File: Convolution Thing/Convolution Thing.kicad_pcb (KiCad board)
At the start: 2 copper layers, 205 parts, among them IC1 PCM3060PW, IC2 SN74LVC1G07DCK3, IC3 LP55231, J1 Eurorack power, J10 In CV 3, J11 In CV 4, J12 In CV 5, J13 In CV 6, J14 In CV 7, J15 In CV 8, J16 LED Header, J17 USB_A, J18 Gate In 1, J19 Gate In 2, J2 Power Header, J20 Gate In 3, J21 Gate In 4, J22 CM4 Pins 1-100, J23 CM4 Pins 101-200, J24 OLED Pins 1-20, J25 OLED Pins 21-40, J3 GPIO Header, J4 Out Left, J5 Out Right, J6 In Left, J7 In Right, J8 In CV 1, J9 In CV 2, Q1 NPN, Q2 NPN, Q3 NPN, Q4 NPN, U1 Compute Module 4, U10 LM4040DBZ-2.5, U11 LM4040DBZ-2.5, U2 TLV1117-50, U3 ADP2303ARDZ-5.0, U4 NE5532, U5 NE5532, U6 NE5532, U7 LTC2309_TSSOP, U8 MCP6004, U9 MCP6004

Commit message: PCB layout work and related changes to the schematic
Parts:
- removed the C13 at (89.5, 92.8)
- removed the C16 at (98.7, 82.3)
- removed the C17 at (180.0, 137.4)
- removed the C18 at (218.5, 117.6)
- removed the C27 at (267.1, 26.6)
- removed the C33 at (187.7, 82.3)
- removed the C34 at (187.7, 85.4)
- removed the C35 at (192.2, 82.3)
- removed the C36 at (187.7, 88.4)
- removed the C52 at (167.6, 69.9)
- removed the C53 at (207.9, 29.6)
- removed the C61 at (167.6, 66.9)
- removed the C64 at (88.9, 144.6)
- removed the C8 at (88.9, 96.4)
- removed the J15 at (144.2, 34.2)
- removed the J20 at (230.4, 156.5)
- removed the J21 at (249.3, 136.8)
- removed the R2 at (188.9, 136.7)
- removed the R21 at (267.1, 32.6)
- removed the R22 at (192.2, 85.3)
- removed the R3 at (189.1, 133.6)
- removed the TP10 at (248.7, 78.5)
- removed the TP8 at (258.8, 78.5)
- removed the U2 at (70.4, 112.4)
- removed the U6 at (231.3, 42.9)
- added C19: 100nF, Capacitor_SMD:C_0805_2012Metric, F.Cu at (227.9, 221.3)
- added C25: 10uF, Capacitor_SMD:C_0805_2012Metric, F.Cu at (157.6, 235.1)
- added C26: 330pF, Capacitor_SMD:C_0805_2012Metric, F.Cu at (158.1, 216.1)
- added C31: 100nF, Capacitor_SMD:C_0805_2012Metric, F.Cu at (22.6, 35.5)
- added C32: 2.2uF, Capacitor_SMD:C_0805_2012Metric, F.Cu at (18.1, 41.6)
- added C57: 100nF, Capacitor_SMD:C_0805_2012Metric, F.Cu at (237.4, 119.1)
- added C59: 470nF, Capacitor_SMD:C_0805_2012Metric, F.Cu at (43.4, 132.5)
- added C60: 100nF, Capacitor_SMD:C_0805_2012Metric, F.Cu at (41.2, 135.6)
- added C65: 100nF, Capacitor_SMD:C_0805_2012Metric, F.Cu at (27.4, 155.3)
- added C66: 100nF, Capacitor_SMD:C_0805_2012Metric, F.Cu at (30.9, 164.5)
- added C67: 10uF, Capacitor_SMD:C_0805_2012Metric, F.Cu at (30.9, 162.5)
- added C9: 100nF, Capacitor_SMD:C_0805_2012Metric, F.Cu at (163.1, 167.4)
- added D10: LED 7, LED_SMD:LED_0805_2012Metric, F.Cu at (53.6, 125.2)
- added D11: LED 8, LED_SMD:LED_0805_2012Metric, F.Cu at (55.7, 125.2)
- added D12: LED 9, LED_SMD:LED_0805_2012Metric, F.Cu at (57.8, 125.2)
- added D13: Activity LED, LED_SMD:LED_0805_2012Metric, F.Cu at (33.4, 116.5)
- added D14: Power LED, LED_SMD:LED_0805_2012Metric, F.Cu at (38.0, 112.8)
- added D6: LED 3, LED_SMD:LED_0805_2012Metric, F.Cu at (45.2, 125.2)
- added D7: LED 4, LED_SMD:LED_0805_2012Metric, F.Cu at (47.3, 125.2)
- added D8: LED 5, LED_SMD:LED_0805_2012Metric, F.Cu at (49.4, 125.2)
- added D9: LED 6, LED_SMD:LED_0805_2012Metric, F.Cu at (51.5, 125.2)
- added J17: Gate In 2, Connector_Audio:Jack_3.5mm_QingPu_WQP-PJ398SM_Vertical_CircularHoles, F.Cu at (80.9, -14.8)
- added J24: GPIO Header, Connector_PinHeader_2.54mm:PinHeader_2x07_P2.54mm_Vertical, F.Cu at (72.1, 160.8)
- added R18: 100k, Resistor_SMD:R_0805_2012Metric, F.Cu at (157.6, 228.5)
- added R19: 22k, Resistor_SMD:R_0805_2012Metric, F.Cu at (158.1, 223.2)
- added R55: 100, Resistor_SMD:R_0805_2012Metric, F.Cu at (42.4, 112.8)
- added R56: 100, Resistor_SMD:R_0805_2012Metric, F.Cu at (33.3, 119.5)
- added TP16: CV4 TP, TestPoint:TestPoint_Loop_D2.60mm_Drill1.6mm_Beaded, F.Cu at (300.2, 91.8)
- added TP18: CV6 TP, TestPoint:TestPoint_Loop_D2.60mm_Drill1.6mm_Beaded, F.Cu at (303.3, 142.7)
- added TP19: CV_SCL TP, TestPoint:TestPoint_Loop_D2.60mm_Drill1.6mm_Beaded, F.Cu at (70.0, 33.7)
- added TP2: PCM_FS TP, TestPoint:TestPoint_Loop_D2.60mm_Drill1.6mm_Beaded, F.Cu at (75.1, 20.5)
- added TP20: CV_SDA TP, TestPoint:TestPoint_Loop_D2.60mm_Drill1.6mm_Beaded, F.Cu at (65.0, 33.7)
- added TP21: CV7 TP, TestPoint:TestPoint_Loop_D2.60mm_Drill1.6mm_Beaded, F.Cu at (263.2, 186.8)
- added TP22: CV8 TP, TestPoint:TestPoint_Loop_D2.60mm_Drill1.6mm_Beaded, F.Cu at (304.1, 187.8)
- added TP25: LED_SCL TP, TestPoint:TestPoint_Loop_D2.60mm_Drill1.6mm_Beaded, F.Cu at (81.9, 28.4)
- added TP26: LED_SDA TP, TestPoint:TestPoint_Loop_D2.60mm_Drill1.6mm_Beaded, F.Cu at (81.9, 33.4)
- added TP28: Gate 2 TP, TestPoint:TestPoint_Loop_D2.60mm_Drill1.6mm_Beaded, F.Cu at (81.9, -20.7)
- added TP29: Gate 3 TP, TestPoint:TestPoint_Loop_D2.60mm_Drill1.6mm_Beaded, F.Cu at (101.2, -20.4)
- added TP30: Gate 4 TP, TestPoint:TestPoint_Loop_D2.60mm_Drill1.6mm_Beaded, F.Cu at (119.2, -19.9)
- added TP31: +3.3V TP, TestPoint:TestPoint_Loop_D2.60mm_Drill1.6mm_Beaded, F.Cu at (63.0, 154.5)
- added U10: Compute Module 4, CM4:Raspberry-Pi-4-Compute-Module, F.Cu at (38.6, 176.4)
- C10: value 100nF -> 22uF
- C12: value 22uF -> 100uF; footprint Capacitor_SMD:C_0805_2012Metric -> Capacitor_SMD:C_1210_3225Metric
- C14: value 10uF -> 47uF
- C23, C7: value 100nF -> 10uF
- C29: value 10uF -> 100nF
- C30: value 330pF -> 2.2uF
- C63: value 470nF -> 100nF
- D4: value Activity LED -> LED 1
- D5: value Power LED -> LED 2
- IC2: value SN74LVC1G07DCK3 -> LP55231; footprint SamacSys:SOT65P210X110-5N -> SamacSys:QFN50P400X400X80-25N
- IC3: value LP55231 -> SN74LVC1G07DCK3; footprint SamacSys:QFN50P400X400X80-25N -> SamacSys:SOT65P210X110-5N
- J1: footprint Connector_PinHeader_2.54mm:PinHeader_2x10_P2.54mm_Vertical_SMD -> Connector_PinHeader_2.54mm:PinHeader_2x05_P2.54mm_Vertical_SMD
- J10: value In CV 3 -> In CV 4; footprint SamacSys:ACJMNV352S -> Connector_Audio:Jack_3.5mm_QingPu_WQP-PJ398SM_Vertical_CircularHoles
- J11: value In CV 4 -> In CV 5; footprint SamacSys:ACJMNV352S -> Connector_Audio:Jack_3.5mm_QingPu_WQP-PJ398SM_Vertical_CircularHoles
- J12: value In CV 5 -> In CV 6; footprint SamacSys:ACJMNV352S -> Connector_Audio:Jack_3.5mm_QingPu_WQP-PJ398SM_Vertical_CircularHoles
- J13: value In CV 6 -> In CV 7; footprint SamacSys:ACJMNV352S -> Connector_Audio:Jack_3.5mm_QingPu_WQP-PJ398SM_Vertical_CircularHoles
- J14: value In CV 7 -> In CV 8; footprint SamacSys:ACJMNV352S -> Connector_Audio:Jack_3.5mm_QingPu_WQP-PJ398SM_Vertical_CircularHoles
- J16: value LED Header -> Gate In 1; footprint Connector_PinHeader_2.54mm:PinHeader_1x09_P2.54mm_Vertical -> Connector_Audio:Jack_3.5mm_QingPu_WQP-PJ398SM_Vertical_CircularHoles
- J18: value Gate In 1 -> Gate In 3; footprint SamacSys:ACJMNV352S -> Connector_Audio:Jack_3.5mm_QingPu_WQP-PJ398SM_Vertical_CircularHoles
- J19: value Gate In 2 -> Gate In 4; footprint SamacSys:ACJMNV352S -> Connector_Audio:Jack_3.5mm_QingPu_WQP-PJ398SM_Vertical_CircularHoles
- J3: value GPIO Header -> Out Left; footprint Connector_PinSocket_2.54mm:PinSocket_1x15_P2.54mm_Vertical -> Connector_Audio:Jack_3.5mm_QingPu_WQP-PJ398SM_Vertical_CircularHoles
- J4: value Out Left -> Out Right; footprint SamacSys:ACJMNV352S -> Connector_Audio:Jack_3.5mm_QingPu_WQP-PJ398SM_Vertical_CircularHoles
- J5: value Out Right -> In Left; footprint SamacSys:ACJMNV352S -> Connector_Audio:Jack_3.5mm_QingPu_WQP-PJ398SM_Vertical_CircularHoles
- J6: value In Left -> In Right; footprint SamacSys:ACJMNV352S -> Connector_Audio:Jack_3.5mm_QingPu_WQP-PJ398SM_Vertical_CircularHoles
- J7: value In Right -> In CV 1; footprint SamacSys:ACJMNV352S -> Connector_Audio:Jack_3.5mm_QingPu_WQP-PJ398SM_Vertical_CircularHoles
- J8: value In CV 1 -> In CV 2; footprint SamacSys:ACJMNV352S -> Connector_Audio:Jack_3.5mm_QingPu_WQP-PJ398SM_Vertical_CircularHoles
- J9: value In CV 2 -> In CV 3; footprint SamacSys:ACJMNV352S -> Connector_Audio:Jack_3.5mm_QingPu_WQP-PJ398SM_Vertical_CircularHoles
- R20: value 100k -> 910k
- TP1: value +5VA TP -> PCM_CLK TP
- TP10: renamed from TP16; value IN L TP -> IN R TP
- TP11: value CV_SCL TP -> DISPLAY_SCL TP
- TP12: value CV_SDA TP -> DISPLAY_SDA TP
- TP13: value CV_SCL TP -> CV1 TP
- TP14: value CV_SDA TP -> CV2 TP
- TP15: value IN L TP -> CV3 TP
- TP17: value CV1 TP -> CV5 TP
- TP27: renamed from TP20; value Gate TP -> Gate 1 TP
- TP3: value PCM_CLK TP -> PCM_DIN TP
- TP4: value PCM_FS TP -> PCM_DOUT TP
- TP5: value PCM_DIN TP -> CODEC_SDA TP
- TP6: value PCM_DOUT TP -> CODEC_SCL TP
- TP7: value CODEC_SDA TP -> +5VA TP
- TP9: value DISPLAY_SCL TP -> IN L TP
- U1: value Compute Module 4 -> TLV1117-50; footprint CM4:Raspberry-Pi-4-Compute-Module -> Package_TO_SOT_SMD:SOT-223
- moved C30 253.7 mm to (18.1, 38.6)
- moved R20 249.1 mm to (22.5, 38.5)
- moved C29 249.1 mm to (18.1, 35.5)
- moved R57 245.8 mm to (70.0, -4.15)
- moved TP27 241.9 mm to (61.3, -20.7)
- moved R61 239.6 mm to (70.2, -15.1)
- moved Q1 231.0 mm to (70.0, -9.48)
- moved R62 227.1 mm to (90.3, -16.3)
- moved J18 226.0 mm to (100.7, -14.8)
- moved R16 223.0 mm to (138.3, 228.0)
- moved R63 220.0 mm to (109.6, -16.1)
- moved Q2 217.5 mm to (89.5, -9.99)
- moved R58 216.5 mm to (89.3, -4.40)
- moved R14 215.2 mm to (248.7, 230.3)
- moved Q3 213.9 mm to (109.3, -9.99)
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- renumbered C15 to C13, C19 to C15, C20 to C16, C21 to C17, C22 to C18, C24 to C20, C25 to C21, C26 to C22, C28 to C24, C31 to C27, C32 to C28, C37 to C33, C38 to C34, C39 to C35, C40 to C36, C41 to C37, C42 to C38, C43 to C39, C44 to C40, C45 to C41, C46 to C42, C47 to C43, C48 to C44, C49 to C45, C50 to C46, C51 to C47, C54 to C50, C55 to C51, C56 to C52, C57 to C53, C59 to C54, C60 to C55, C58 to C56, C62 to C58, C65 to C61, C66 to C62, C67 to C64, C9 to C8, J17 to J15, J22 to J20, J23 to J21, J24 to J22, J25 to J23, R12 to R10, R13 to R11, R14 to R12, R15 to R13, R16 to R14, R17 to R15, R18 to R16, R19 to R17, R4 to R2, R23 to R21, R24 to R22, R25 to R23, R26 to R24, R27 to R25, R28 to R26, R29 to R27, R30 to R28, R31 to R29, R5 to R3, R32 to R30, R33 to R31, R34 to R32, R35 to R33, R36 to R34, R37 to R35, R38 to R36, R39 to R37, R40 to R38, R41 to R39, R6 to R4, R42 to R40, R43 to R41, R44 to R42, R45 to R43, R46 to R44, R47 to R45, R48 to R46, R49 to R47, R50 to R48, R51 to R49, R7 to R5, R52 to R50, R53 to R51, R54 to R52, R55 to R53, R56 to R54, R8 to R6, R9 to R7, R10 to R8, R11 to R9, TP18 to TP23, TP19 to TP24, TP2 to TP8, U3 to U2, U4 to U3, U5 to U4, U7 to U5, U8 to U6, U9 to U7, U10 to U8, U11 to U9
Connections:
- net DAC_VOUT_L+ renamed CODEC_VOUT_L+
- net DAC_VOUT_L- renamed CODEC_VOUT_L-
- net DAC_VOUT_R+ renamed CODEC_VOUT_R+
- net DAC_VOUT_R- renamed CODEC_VOUT_R-
- C11 pad 1: +12V -> GND
- C11 pad 2: GND -> -12V
- C12 pad 1: GND -> +5VA
- C12 pad 2: -12V -> GND
- C14 pad 1: +3V3 -> +5V
- C23 pad 1: -12V -> Net-(C23-Pad1)
- C23 pad 2: GND -> /Audio In/IN_L
- C24 pad 1: ADC_VIN_L -> CODEC_VIN_L
- C29 pad 1: Net-(C29-Pad1) -> +12V
- C29 pad 2: Net-(C29-Pad2) -> GND
- C30 pad 1: ADC_VIN_R -> +12V
- C30 pad 2: Net-(C30-Pad2) -> GND
- C33 pad 1: Net-(C37-Pad1) -> Net-(C33-Pad1)
- C63 pad 1: /LEDs/C2- -> +3V3
- C63 pad 2: /LEDs/C2+ -> GND
- C7 pad 1: +5V -> +12V
- D4 pad 1: Net-(D4-Pad1) -> GND
- D4 pad 2: +3V3 -> /LEDs/D1
- D5 pad 1: Net-(D5-Pad1) -> GND
- D5 pad 2: +3V3 -> /LEDs/D2
- DS1 pad 32: DISPLAY_SCL -> CM4_SCL1
- DS1 pad 33: DISPLAY_SDA -> CM4_SDA1
- DS1 pad 34: DISPLAY_SDA -> CM4_SDA1
- IC1 pad 1: CODEC_SCL -> CM4_SCL0
- IC1 pad 12: DAC_IN -> CM4_PCM_DOUT
- IC1 pad 2: CODEC_SDA -> CM4_SDA0
- IC1 pad 25: ADC_VIN_L -> CODEC_VIN_L
- IC1 pad 26: ADC_VIN_R -> CODEC_VIN_R
- IC1 pad 3: ADC_OUT -> CM4_PCM_DIN
- IC1 pad 4: CODEC_LRCK -> CM4_PCM_FS
- IC1 pad 5: CODEC_BCK -> CM4_PCM_CLK
- IC2 pad 1: Net-(IC2-Pad1) -> /LEDs/C2+
- IC2 pad 2: Net-(IC2-Pad2) -> /LEDs/C1+
- IC2 pad 3: GND -> +5V
- IC2 pad 4: Net-(IC2-Pad4) -> GND
- IC2 pad 5: +3V3 -> +5V
- IC3 pad 1: /LEDs/C2+ -> Net-(IC3-Pad1)
- IC3 pad 2: /LEDs/C1+ -> CM4_LED_POWER
- IC3 pad 3: +5V -> GND
- IC3 pad 4: GND -> Net-(IC3-Pad4)
- IC3 pad 5: +5V -> +3V3
- J15 pad 2: /USB/USB_N -> CM4_USB_N
- J15 pad 3: /USB/USB_P -> CM4_USB_P
- J2 pad 1: +3V3 -> GND
- J2 pad 2: +12V -> -12V
- J2 pad 3: -12V -> +12V
- J2 pad 4: GND -> +3V3
- R15 pad 1: Net-(J5-PadT) -> Net-(J4-PadT)
- R16 pad 1: Net-(C27-Pad1) -> Net-(C23-Pad1)
- R17 pad 2: ADC_VIN_L -> CODEC_VIN_L
- R20 pad 1: Net-(C29-Pad1) -> /Display/IREF
- R20 pad 2: Net-(C30-Pad2) -> GND
- R22 pad 2: Net-(J8-PadT) -> Net-(J7-PadT)
- R24 pad 2: Net-(J9-PadT) -> Net-(J8-PadT)
- R26 pad 2: Net-(J10-PadT) -> Net-(J9-PadT)
- R27 pad 1: Net-(C37-Pad1) -> Net-(C33-Pad1)
- R30 pad 2: Net-(C37-Pad1) -> Net-(C33-Pad1)
- R34 pad 2: Net-(J11-PadT) -> Net-(J10-PadT)
- R36 pad 2: Net-(J12-PadT) -> Net-(J11-PadT)
- R38 pad 2: Net-(J13-PadT) -> Net-(J12-PadT)
- R46 pad 2: Net-(J14-PadT) -> Net-(J13-PadT)
- R48 pad 2: Net-(J15-PadT) -> Net-(J14-PadT)
- R57 pad 2: Net-(J18-PadT) -> Net-(J16-PadT)
- R59 pad 2: Net-(J20-PadT) -> Net-(J18-PadT)
- R60 pad 2: Net-(J21-PadT) -> Net-(J19-PadT)
- R8 pad 1: Net-(J4-PadT) -> Net-(J3-PadT)
- TP1 pad 1: +5VA -> CM4_PCM_CLK
- TP10 pad 1: ADC_VIN_R -> CODEC_VIN_R
- TP11 pad 1: CV_SCL -> CM4_SCL1
- TP12 pad 1: CV_SDA -> CM4_SDA1
- TP13 pad 1: LED_SCL -> /CV/CH0
- TP14 pad 1: LED_SDA -> /CV/CH1
- TP15 pad 1: ADC_VIN_L -> /CV/CH2
- TP17 pad 1: Net-(C37-Pad1) -> /CV/CH4
- TP3 pad 1: CODEC_BCK -> CM4_PCM_DIN
- TP4 pad 1: CODEC_LRCK -> CM4_PCM_DOUT
- TP5 pad 1: ADC_OUT -> CM4_SDA0
- TP6 pad 1: DAC_IN -> CM4_SCL0
- TP7 pad 1: CODEC_SDA -> +5VA
- TP9 pad 1: DISPLAY_SCL -> CODEC_VIN_L
- U1 pad 2: GND -> +5VA
- U1 pad 3: (no net) -> +12V
- U4 pad 1: ADC_VIN_L -> CODEC_VIN_L
- U4 pad 5: (no net) -> CODEC_VCOM
- U4 pad 6: (no net) -> Net-(C26-Pad2)
- U4 pad 7: (no net) -> CODEC_VIN_R
- U5 pad 6: CV_SCL -> CM4_SCL3
- U5 pad 7: CV_SDA -> CM4_SDA3
- U6 pad 1: Net-(C37-Pad1) -> Net-(C33-Pad1)
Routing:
- net GND: track 0.00 -> 170.5 mm, vias 0 -> 104
- net +5V: track 0.00 -> 121.8 mm, vias 0 -> 2
- net +3V3: track 0.00 -> 78.1 mm, vias 0 -> 2
- net +12V: track 0.00 -> 59.3 mm
- net CM4_SCL0: track 0.00 -> 56.7 mm, vias 0 -> 2
- net CM4_SDA0: track 0.00 -> 54.9 mm
- net CM4_SCL3: track 0.00 -> 44.9 mm, vias 0 -> 2
- net CM4_SDA3: track 0.00 -> 42.3 mm, vias 0 -> 2
- net CM4_PCM_FS: track 0.00 -> 42.1 mm
- net CM4_PCM_CLK: track 0.00 -> 35.1 mm
- net CM4_PCM_DIN: track 0.00 -> 34.2 mm, vias 0 -> 2
- net CM4_USB_N: track 0.00 -> 31.9 mm
- net CM4_USB_P: track 0.00 -> 31.9 mm
- net CM4_PCM_DOUT: track 0.00 -> 28.7 mm
- net -12V: track 0.00 -> 24.8 mm
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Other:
- copper layers 2 -> 4
- net class Default: clearance 0.2 -> 0.1; via_dia 0.8 -> 0.45; via_drill 0.4 -> 0.25
- rule trace_clearance: 0.2 -> 0.1
- rule via_min_drill: 0.3 -> 0.2
- rule via_min_size: 0.4 -> 0.25

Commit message: PCB layout
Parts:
- removed J22: OLED Pins 1-20, Connector_PinHeader_2.54mm:PinHeader_1x20_P2.54mm_Vertical
- removed J23: OLED Pins 21-40, Connector_PinHeader_2.54mm:PinHeader_1x20_P2.54mm_Vertical
- J24: footprint Connector_PinHeader_2.54mm:PinHeader_2x07_P2.54mm_Vertical -> Connector_PinSocket_2.54mm:PinSocket_2x07_P2.54mm_Vertical
- moved H4 271.1 mm to (188.0, 201.0)
- moved J20 214.4 mm to (38.2, 193.4), turned to 180 degrees
- moved H3 211.9 mm to (11.0, 201.0)
- moved H2 205.2 mm to (188.0, 69.0)
- moved TP14 195.7 mm to (109.5, 90.8)
- moved TP16 191.9 mm to (109.2, 110.2)
- moved TP27 187.6 mm to (125.5, 155.6)
- moved C54 187.5 mm to (100.0, 102.5), turned to 270 degrees
- moved C37 186.8 mm to (113.6, 89.8)
- moved R31 185.6 mm to (113.6, 91.9)
- moved TP28 185.6 mm to (140.1, 155.6)
- moved R23 185.2 mm to (112.7, 98.6), turned to 270 degrees
- moved R61 184.8 mm to (125.2, 161.4), turned to 180 degrees
- moved R33 184.7 mm to (112.5, 118.0), turned to 270 degrees
- moved J21 184.7 mm to (38.6, 159.4), turned to 180 degrees
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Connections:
- U1 pad 4: (no net) -> +5VA
- U6 pad 13: Net-(C42-Pad2) -> Net-(C34-Pad2)
- U6 pad 14: Net-(C42-Pad1) -> Net-(C34-Pad1)
- U6 pad 6: Net-(C34-Pad2) -> Net-(C35-Pad2)
- U6 pad 7: Net-(C34-Pad1) -> Net-(C35-Pad1)
- U6 pad 8: Net-(C35-Pad1) -> Net-(C42-Pad1)
- U6 pad 9: Net-(C35-Pad2) -> Net-(C42-Pad2)
- U7 pad 13: Net-(C51-Pad2) -> Net-(C44-Pad2)
- U7 pad 14: Net-(C51-Pad1) -> Net-(C44-Pad1)
- U7 pad 6: Net-(C44-Pad2) -> Net-(C50-Pad2)
- U7 pad 7: Net-(C44-Pad1) -> Net-(C50-Pad1)
- U7 pad 8: Net-(C50-Pad1) -> Net-(C51-Pad1)
- U7 pad 9: Net-(C50-Pad2) -> Net-(C51-Pad2)
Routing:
- net +12V: track 59.3 -> 453.6 mm, vias 0 -> 5
- net +3V3: track 78.1 -> 345.2 mm, vias 2 -> 4
- net -12V: track 24.8 -> 267.8 mm, vias 0 -> 6
- net /CV/VREF_-2.5: track 0.00 -> 214.6 mm
- net GATE_IN_4: track 0.00 -> 153.9 mm, vias 0 -> 6
- net GATE_IN_3: track 0.00 -> 148.6 mm, vias 0 -> 4
- net +5VA: track 4.77 -> 152.1 mm, vias 0 -> 7
- net GATE_IN_2: track 0.00 -> 126.8 mm, vias 0 -> 4
- net /CV/CH5: track 0.00 -> 123.5 mm, vias 0 -> 1
- net /CV/CH4: track 0.00 -> 118.1 mm, vias 0 -> 1
- net GATE_IN_1: track 0.00 -> 109.3 mm, vias 0 -> 4
- net /CV/CH7: track 0.00 -> 106.8 mm, vias 0 -> 1
- net CODEC_VOUT_R-: track 0.00 -> 106.8 mm, vias 0 -> 5
- net CODEC_VOUT_R+: track 0.00 -> 102.0 mm, vias 0 -> 4
- net /CV/CH6: track 0.00 -> 100.1 mm, vias 0 -> 1
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- added copper zone on Gnd.Cu, net GND
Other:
- board outline added: 189 x 145 mm

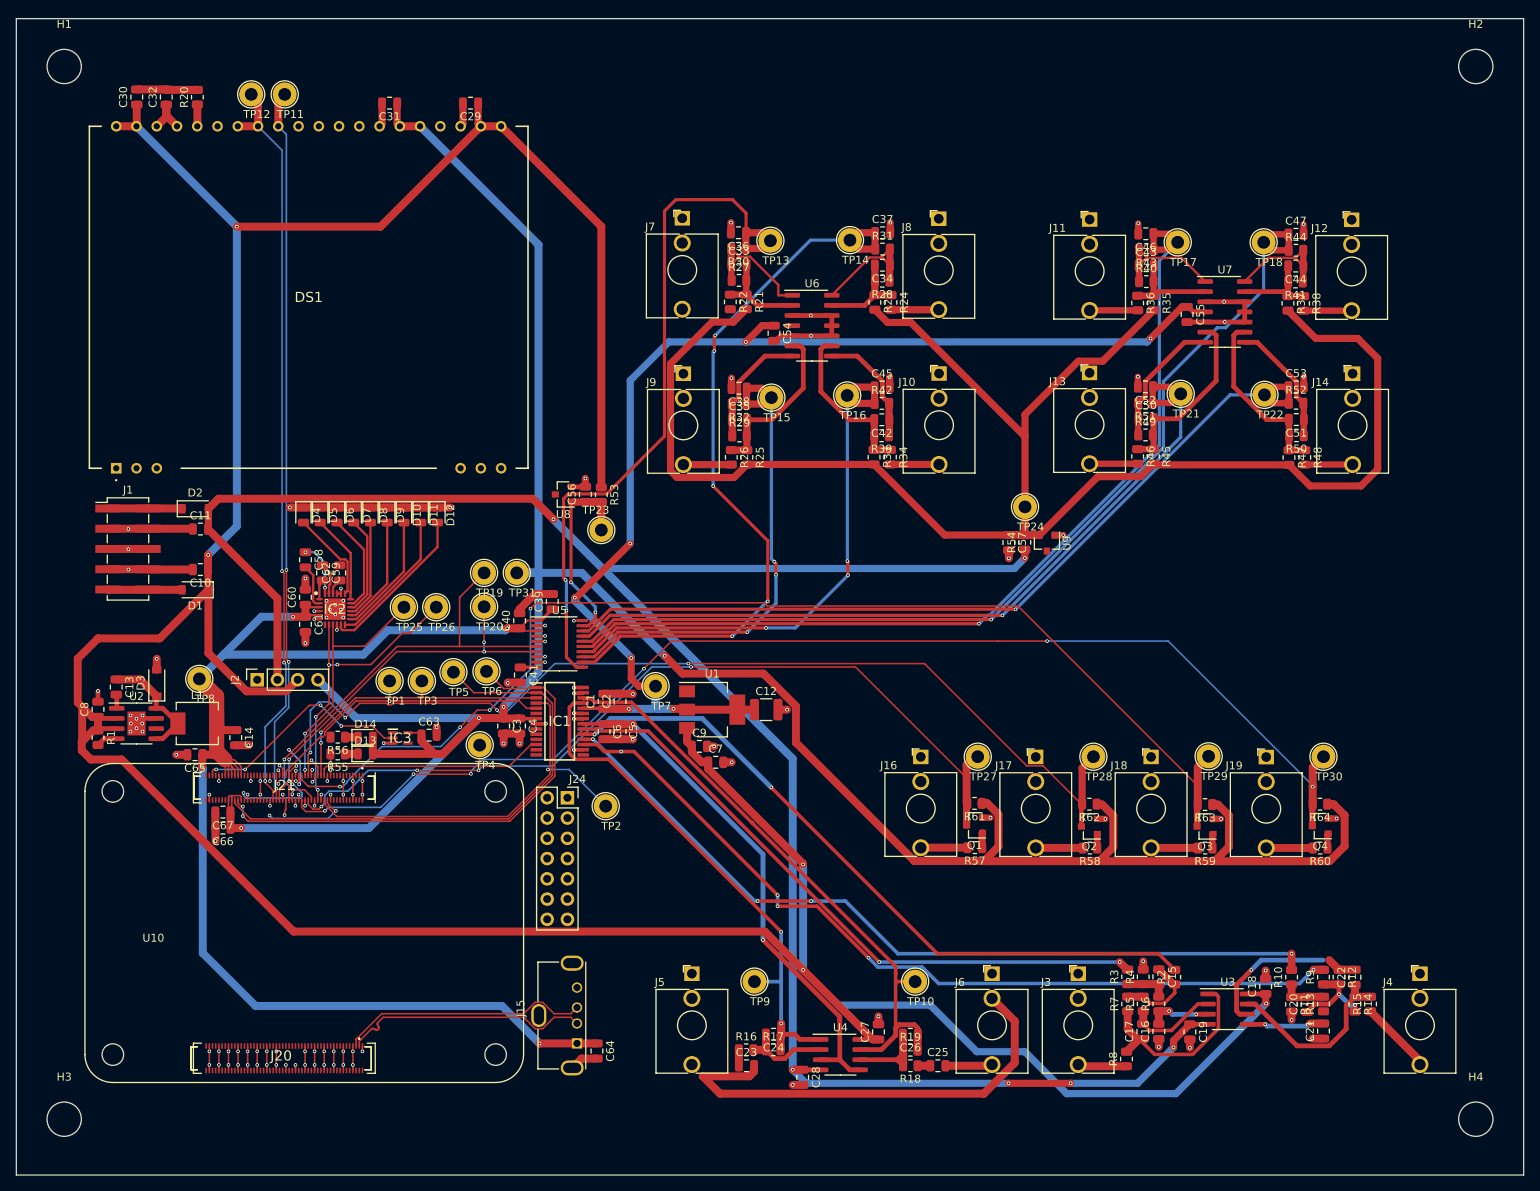
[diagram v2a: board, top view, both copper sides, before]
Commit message: Entirely new, simpler PCB
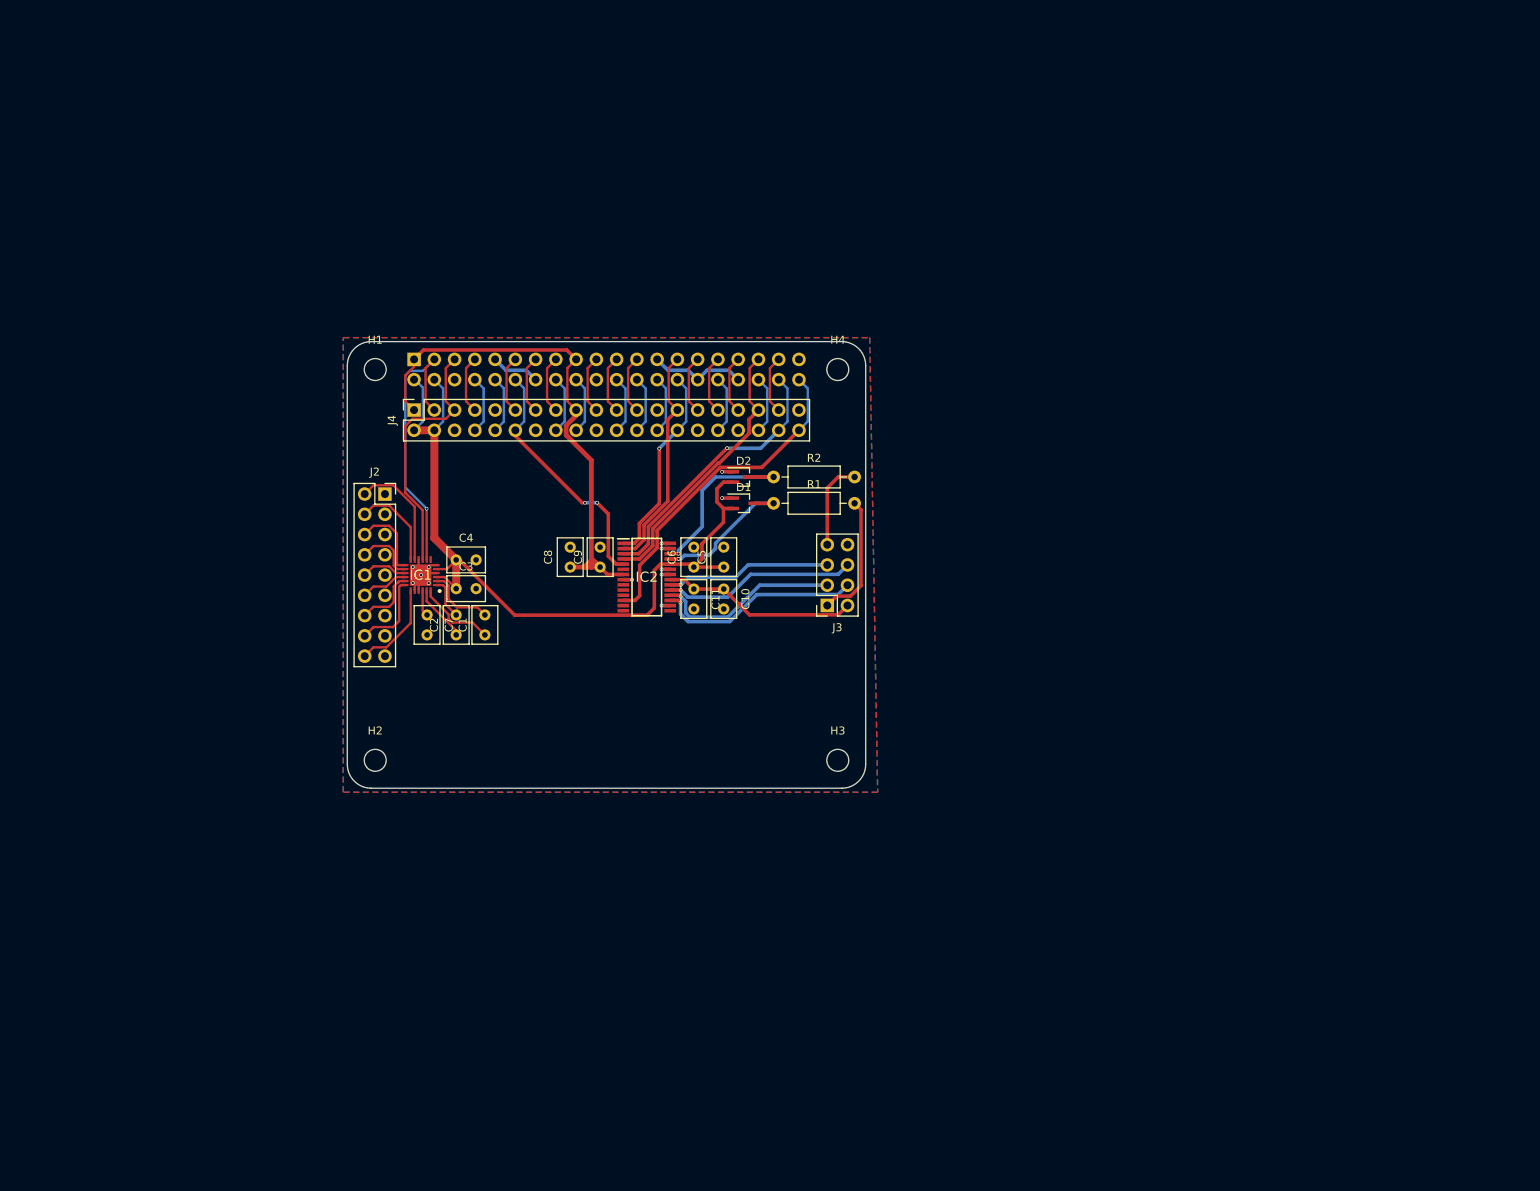
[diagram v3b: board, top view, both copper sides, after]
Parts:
- removed C12: 100uF, Capacitor_SMD:C_1210_3225Metric
- removed C13, C18, C19, C27, C28, C29, C31, C40, C41, C54, C55, C56, C57, C60, C63, C64, C65, C66: 100nF, Capacitor_SMD:C_0805_2012Metric
- removed C14: 47uF, Capacitor_SMD:C_0805_2012Metric
- removed C15, C20: 4.7nF, Capacitor_SMD:C_0805_2012Metric
- removed C16, C17, C21, C22: 470pF, Capacitor_SMD:C_0805_2012Metric
- removed C23, C25, C39, C67: 10uF, Capacitor_SMD:C_0805_2012Metric
- removed C24, C26, C33, C34, C35, C42, C43, C44, C50, C51: 330pF, Capacitor_SMD:C_0805_2012Metric
- removed C30, C32: 2.2uF, Capacitor_SMD:C_0805_2012Metric
- removed C36, C37, C38, C45, C46, C47, C52, C53: 2nF, Capacitor_SMD:C_0805_2012Metric
- removed C58, C59: 470nF, Capacitor_SMD:C_0805_2012Metric
- removed C61, C62: 1uF, Capacitor_SMD:C_0805_2012Metric
- removed D10: LED 7, LED_SMD:LED_0805_2012Metric
- removed D11: LED 8, LED_SMD:LED_0805_2012Metric
- removed D12: LED 9, LED_SMD:LED_0805_2012Metric
- removed D13: Activity LED, LED_SMD:LED_0805_2012Metric
- removed D14: Power LED, LED_SMD:LED_0805_2012Metric
- removed D3: Catch Diode, Diode_SMD:D_SOD-123
- removed D4: LED 1, LED_SMD:LED_0805_2012Metric
- removed D5: LED 2, LED_SMD:LED_0805_2012Metric
- removed D6: LED 3, LED_SMD:LED_0805_2012Metric
- removed D7: LED 4, LED_SMD:LED_0805_2012Metric
- removed D8: LED 5, LED_SMD:LED_0805_2012Metric
- removed D9: LED 6, LED_SMD:LED_0805_2012Metric
- removed DS1: EA_OLEDM128-6GGA, SamacSys:EAOLEDM1286GGA
- removed IC3: SN74LVC1G07DCK3, SamacSys:SOT65P210X110-5N
- removed J10: In CV 4, Connector_Audio:Jack_3.5mm_QingPu_WQP-PJ398SM_Vertical_CircularHoles
- removed J11: In CV 5, Connector_Audio:Jack_3.5mm_QingPu_WQP-PJ398SM_Vertical_CircularHoles
- removed J12: In CV 6, Connector_Audio:Jack_3.5mm_QingPu_WQP-PJ398SM_Vertical_CircularHoles
- removed J13: In CV 7, Connector_Audio:Jack_3.5mm_QingPu_WQP-PJ398SM_Vertical_CircularHoles
- removed J14: In CV 8, Connector_Audio:Jack_3.5mm_QingPu_WQP-PJ398SM_Vertical_CircularHoles
- removed J15: USB_A, Connector_USB:USB_A_Molex_105057_Vertical
- removed J16: Gate In 1, Connector_Audio:Jack_3.5mm_QingPu_WQP-PJ398SM_Vertical_CircularHoles
- removed J17: Gate In 2, Connector_Audio:Jack_3.5mm_QingPu_WQP-PJ398SM_Vertical_CircularHoles
- removed J18: Gate In 3, Connector_Audio:Jack_3.5mm_QingPu_WQP-PJ398SM_Vertical_CircularHoles
- removed J19: Gate In 4, Connector_Audio:Jack_3.5mm_QingPu_WQP-PJ398SM_Vertical_CircularHoles
- removed J20: CM4 Pins 1-100, SamacSys:DF40C100DS04V58
- removed J21: CM4 Pins 101-200, SamacSys:DF40C100DS04V58
- removed J24: GPIO Header, Connector_PinSocket_2.54mm:PinSocket_2x07_P2.54mm_Vertical
- removed J5: In Left, Connector_Audio:Jack_3.5mm_QingPu_WQP-PJ398SM_Vertical_CircularHoles
- removed J6: In Right, Connector_Audio:Jack_3.5mm_QingPu_WQP-PJ398SM_Vertical_CircularHoles
- removed J7: In CV 1, Connector_Audio:Jack_3.5mm_QingPu_WQP-PJ398SM_Vertical_CircularHoles
- removed J8: In CV 2, Connector_Audio:Jack_3.5mm_QingPu_WQP-PJ398SM_Vertical_CircularHoles
- removed J9: In CV 3, Connector_Audio:Jack_3.5mm_QingPu_WQP-PJ398SM_Vertical_CircularHoles
- removed L1: 4.7uH, Inductor_SMD:L_Vishay_IHLP-2020
- removed Q1, Q2, Q3, Q4: NPN, Package_TO_SOT_SMD:SOT-23
- removed R10, R3, R9: 12k, Resistor_SMD:R_0805_2012Metric
- removed R11, R14, R4, R7: 15k, Resistor_SMD:R_0805_2012Metric
- removed R12, R13, R5, R6: 820, Resistor_SMD:R_0805_2012Metric
- removed R15, R8: 1k, Resistor_SMD:R_0805_2012Metric
- removed R16, R18, R22, R24, R26, R34, R36, R38, R46, R48, R57, R58, R59, R60: 100k, Resistor_SMD:R_0805_2012Metric
- removed R17, R19: 22k, Resistor_SMD:R_0805_2012Metric
- removed R20: 910k, Resistor_SMD:R_0805_2012Metric
- removed R21, R23, R25, R27, R28, R29, R33, R35, R37, R39, R40, R41, R45, R47, R49, R50: 50k, Resistor_SMD:R_0805_2012Metric
- removed R30, R31, R32, R42, R43, R44, R51, R52: 47, Resistor_SMD:R_0805_2012Metric
- removed R53, R54: 2k, Resistor_SMD:R_0805_2012Metric
- removed R55, R56: 100, Resistor_SMD:R_0805_2012Metric
- removed R61, R62, R63, R64: 10k, Resistor_SMD:R_0805_2012Metric
- removed TP1: PCM_CLK TP, TestPoint:TestPoint_Loop_D2.60mm_Drill1.6mm_Beaded
- removed TP10: IN R TP, TestPoint:TestPoint_Loop_D2.60mm_Drill1.6mm_Beaded
- removed TP11: DISPLAY_SCL TP, TestPoint:TestPoint_Loop_D2.60mm_Drill1.6mm_Beaded
- removed TP12: DISPLAY_SDA TP, TestPoint:TestPoint_Loop_D2.60mm_Drill1.6mm_Beaded
- removed TP13: CV1 TP, TestPoint:TestPoint_Loop_D2.60mm_Drill1.6mm_Beaded
- removed TP14: CV2 TP, TestPoint:TestPoint_Loop_D2.60mm_Drill1.6mm_Beaded
- removed TP15: CV3 TP, TestPoint:TestPoint_Loop_D2.60mm_Drill1.6mm_Beaded
- removed TP16: CV4 TP, TestPoint:TestPoint_Loop_D2.60mm_Drill1.6mm_Beaded
- removed TP17: CV5 TP, TestPoint:TestPoint_Loop_D2.60mm_Drill1.6mm_Beaded
- removed TP18: CV6 TP, TestPoint:TestPoint_Loop_D2.60mm_Drill1.6mm_Beaded
- removed TP19: CV_SCL TP, TestPoint:TestPoint_Loop_D2.60mm_Drill1.6mm_Beaded
- removed TP2: PCM_FS TP, TestPoint:TestPoint_Loop_D2.60mm_Drill1.6mm_Beaded
- removed TP20: CV_SDA TP, TestPoint:TestPoint_Loop_D2.60mm_Drill1.6mm_Beaded
- removed TP21: CV7 TP, TestPoint:TestPoint_Loop_D2.60mm_Drill1.6mm_Beaded
- removed TP22: CV8 TP, TestPoint:TestPoint_Loop_D2.60mm_Drill1.6mm_Beaded
- removed TP23: +2.5V TP, TestPoint:TestPoint_Loop_D2.60mm_Drill1.6mm_Beaded
- removed TP24: -2.5V TP, TestPoint:TestPoint_Loop_D2.60mm_Drill1.6mm_Beaded
- removed TP25: LED_SCL TP, TestPoint:TestPoint_Loop_D2.60mm_Drill1.6mm_Beaded
- removed TP26: LED_SDA TP, TestPoint:TestPoint_Loop_D2.60mm_Drill1.6mm_Beaded
- removed TP27: Gate 1 TP, TestPoint:TestPoint_Loop_D2.60mm_Drill1.6mm_Beaded
- removed TP28: Gate 2 TP, TestPoint:TestPoint_Loop_D2.60mm_Drill1.6mm_Beaded
- removed TP29: Gate 3 TP, TestPoint:TestPoint_Loop_D2.60mm_Drill1.6mm_Beaded
- removed TP3: PCM_DIN TP, TestPoint:TestPoint_Loop_D2.60mm_Drill1.6mm_Beaded
- removed TP30: Gate 4 TP, TestPoint:TestPoint_Loop_D2.60mm_Drill1.6mm_Beaded
- removed TP31: +3.3V TP, TestPoint:TestPoint_Loop_D2.60mm_Drill1.6mm_Beaded
- removed TP4: PCM_DOUT TP, TestPoint:TestPoint_Loop_D2.60mm_Drill1.6mm_Beaded
- removed TP5: CODEC_SDA TP, TestPoint:TestPoint_Loop_D2.60mm_Drill1.6mm_Beaded
- removed TP6: CODEC_SCL TP, TestPoint:TestPoint_Loop_D2.60mm_Drill1.6mm_Beaded
- removed TP7: +5VA TP, TestPoint:TestPoint_Loop_D2.60mm_Drill1.6mm_Beaded
- removed TP8: +5V TP, TestPoint:TestPoint_Loop_D2.60mm_Drill1.6mm_Beaded
- removed TP9: IN L TP, TestPoint:TestPoint_Loop_D2.60mm_Drill1.6mm_Beaded
- removed U1: TLV1117-50, Package_TO_SOT_SMD:SOT-223
- removed U10: Compute Module 4, CM4:Raspberry-Pi-4-Compute-Module
- removed U2: ADP2303ARDZ-5.0, Package_SO:SOIC-8-1EP_3.9x4.9mm_P1.27mm_EP2.29x3mm
- removed U3, U4: NE5532, Package_SO:SOIC-8_3.9x4.9mm_P1.27mm
- removed U5: LTC2309_TSSOP, Package_SO:TSSOP-20_4.4x6.5mm_P0.65mm
- removed U6, U7: MCP6004, Package_SO:SOIC-14_3.9x8.7mm_P1.27mm
- removed U8, U9: LM4040DBZ-2.5, Package_TO_SOT_SMD:SOT-23
- C1: value 10uF -> 470nF; footprint Capacitor_SMD:C_0805_2012Metric -> Capacitor_THT:C_Rect_L4.6mm_W3.0mm_P2.50mm_MKS02_FKP02
- C10: value 22uF -> 10uF; footprint Capacitor_SMD:C_0805_2012Metric -> Capacitor_THT:C_Rect_L4.6mm_W3.0mm_P2.50mm_MKS02_FKP02
- C11: value 22uF -> 100nF; footprint Capacitor_SMD:C_0805_2012Metric -> Capacitor_THT:C_Rect_L4.6mm_W3.0mm_P2.50mm_MKS02_FKP02
- C2: value 100nF -> 470nF; footprint Capacitor_SMD:C_0805_2012Metric -> Capacitor_THT:C_Rect_L4.6mm_W3.0mm_P2.50mm_MKS02_FKP02
- C3: value 10uF -> 100nF; footprint Capacitor_SMD:C_0805_2012Metric -> Capacitor_THT:C_Rect_L4.6mm_W3.0mm_P2.50mm_MKS02_FKP02
- C4: value 100nF -> 1uF; footprint Capacitor_SMD:C_0805_2012Metric -> Capacitor_THT:C_Rect_L4.6mm_W3.0mm_P2.50mm_MKS02_FKP02
- C5, C6, C9: footprint Capacitor_SMD:C_0805_2012Metric -> Capacitor_THT:C_Rect_L4.6mm_W3.0mm_P2.50mm_MKS02_FKP02
- C7: value 10uF -> 1uF; footprint Capacitor_SMD:C_0805_2012Metric -> Capacitor_THT:C_Rect_L4.6mm_W3.0mm_P2.50mm_MKS02_FKP02
- C8: value 100nF -> 10uF; footprint Capacitor_SMD:C_0805_2012Metric -> Capacitor_THT:C_Rect_L4.6mm_W3.0mm_P2.50mm_MKS02_FKP02
- D1, D2: value Schottky -> BAT54S; footprint Diode_SMD:D_SOD-123 -> Package_TO_SOT_SMD:SOT-323_SC-70_Handsoldering
- H1, H2, H3, H4: footprint MountingHole:MountingHole_4.3mm_M4 -> Omat:MountingHole_2.75mm_M2.5
- IC1: value PCM3060PW -> LP55231; footprint SamacSys:SOP65P640X120-28N -> SamacSys:QFN50P400X400X80-25N
- IC2: value LP55231 -> PCM3060PW; footprint SamacSys:QFN50P400X400X80-25N -> SamacSys:SOP65P640X120-28N
- J1: value Eurorack power -> GPIO Header; footprint Connector_PinHeader_2.54mm:PinHeader_2x05_P2.54mm_Vertical_SMD -> Connector_PinHeader_2.54mm:PinHeader_2x20_P2.54mm_Vertical; moved to B.Cu
- J2: value Power Header -> LED Socket; footprint Connector_PinSocket_2.54mm:PinSocket_1x04_P2.54mm_Vertical -> Connector_PinSocket_2.54mm:PinSocket_2x09_P2.54mm_Vertical
- J3: value Out Left -> Audio IO Socket; footprint Connector_Audio:Jack_3.5mm_QingPu_WQP-PJ398SM_Vertical_CircularHoles -> Connector_PinSocket_2.54mm:PinSocket_2x04_P2.54mm_Vertical
- J4: value Out Right -> GPIO Socket; footprint Connector_Audio:Jack_3.5mm_QingPu_WQP-PJ398SM_Vertical_CircularHoles -> Connector_PinSocket_2.54mm:PinSocket_2x20_P2.54mm_Vertical
- R1: value 100k -> 100; footprint Resistor_SMD:R_0805_2012Metric -> Resistor_THT:R_Axial_DIN0207_L6.3mm_D2.5mm_P10.16mm_Horizontal
- R2: value 12k -> 100; footprint Resistor_SMD:R_0805_2012Metric -> Resistor_THT:R_Axial_DIN0207_L6.3mm_D2.5mm_P10.16mm_Horizontal
- moved H2 163.1 mm to (50.0, 156.0)
- moved J4 144.6 mm to (54.9, 112.1), turned to 90 degrees
- moved H4 123.4 mm to (108.0, 107.0)
- moved H3 106.9 mm to (108.0, 156.0)
- moved R1 89.7 mm to (100.0, 123.8), turned to 0 degrees
- moved R2 80.4 mm to (100.0, 120.5), turned to 0 degrees
- moved D1 69.6 mm to (96.2, 123.8), turned to 0 degrees
- moved D2 68.9 mm to (96.2, 120.5)
- moved C10 65.7 mm to (93.7, 134.5), turned to 270 degrees
- moved C11 62.3 mm to (90.0, 134.5), turned to 270 degrees
- moved C8 61.8 mm to (74.5, 131.8)
- moved J3 55.9 mm to (106.7, 136.6), turned to 180 degrees
- moved H1 54.5 mm to (50.0, 107.0)
- moved J1 43.0 mm to (54.9, 105.7), turned to 270 degrees
- moved C7 40.6 mm to (56.5, 137.8), turned to 270 degrees
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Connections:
- C1 pad 1: +5VA -> /C1-
- C1 pad 2: GND -> /C1+
- C10 pad 1: +12V -> /CODEC_VCOM
- C11 pad 1: GND -> /CODEC_VCOM
- C11 pad 2: -12V -> GND
- C2 pad 1: +5VA -> /C2-
- C2 pad 2: GND -> /C2+
- C3 pad 1: +3V3 -> +5V
- C4 pad 1: +3V3 -> +5V
- C5 pad 1: CODEC_VCOM -> +5V
- C6 pad 1: CODEC_VCOM -> +5V
- C7 pad 1: +12V -> /LED_VOUT
- C8 pad 1: +12V -> +3V3
- C9 pad 1: +12V -> +3V3
- D1 pad 1: +12V -> GND
- D1 pad 2: Net-(D1-Pad2) -> +5V
- D2 pad 1: Net-(D2-Pad1) -> GND
- D2 pad 2: -12V -> +5V
- IC1 pad 1: CM4_SCL0 -> /C2+
- IC1 pad 10: Net-(IC1-Pad10) -> GND
- IC1 pad 11: Net-(IC1-Pad11) -> /D9
- IC1 pad 12: CM4_PCM_DOUT -> /D8
- IC1 pad 13: Net-(IC1-Pad13) -> /D7
- IC1 pad 14: Net-(IC1-Pad14) -> /D6
- IC1 pad 15: Net-(IC1-Pad15) -> /D5
- IC1 pad 16: GND -> /D4
- IC1 pad 17: CODEC_VOUT_R- -> /D3
- IC1 pad 18: CODEC_VOUT_R+ -> /D2
- IC1 pad 19: CODEC_VOUT_L- -> /D1
- IC1 pad 2: CM4_SDA0 -> /C1+
- IC1 pad 20: CODEC_VOUT_L+ -> GND
- IC1 pad 21: CODEC_VCOM -> GND
- IC1 pad 22: GND -> /LED_VOUT
- IC1 pad 23: GND -> /C2-
- IC1 pad 24: +5VA -> /C1-
- IC1 pad 25: CODEC_VIN_L -> GND
- IC1 pad 3: CM4_PCM_DIN -> +5V
- IC1 pad 4: CM4_PCM_FS -> GND
- IC1 pad 5: CM4_PCM_CLK -> +5V
- IC1 pad 6: Net-(IC1-Pad6) -> GND
- IC1 pad 7: +3V3 -> Net-(IC1-Pad7)
- IC1 pad 8: GND -> /SDA1
- IC1 pad 9: Net-(IC1-Pad9) -> /SCL1
- IC2 pad 1: /LEDs/C2+ -> /SCL0
- IC2 pad 10: GND -> Net-(IC2-Pad10)
- IC2 pad 11: /LEDs/D9 -> Net-(IC2-Pad11)
- IC2 pad 12: /LEDs/D8 -> /PCM_DOUT
- IC2 pad 13: /LEDs/D7 -> Net-(IC2-Pad13)
- IC2 pad 14: /LEDs/D6 -> Net-(IC2-Pad14)
- IC2 pad 15: /LEDs/D5 -> Net-(IC2-Pad15)
- IC2 pad 16: /LEDs/D4 -> GND
- IC2 pad 17: /LEDs/D3 -> /CODEC_OUT_R-
- IC2 pad 18: /LEDs/D2 -> /CODEC_OUT_R+
- IC2 pad 19: /LEDs/D1 -> /CODEC_OUT_L-
- IC2 pad 2: /LEDs/C1+ -> /SDA0
- IC2 pad 20: GND -> /CODEC_OUT_L+
- IC2 pad 21: GND -> /CODEC_VCOM
- IC2 pad 22: /LEDs/VOUT -> GND
- IC2 pad 23: /LEDs/C2- -> GND
- IC2 pad 24: /LEDs/C1- -> +5V
- IC2 pad 25: GND -> /CODEC_IN_L
- IC2 pad 3: +5V -> /PCM_DIN
- IC2 pad 4: GND -> /PCM_FS
- IC2 pad 5: +5V -> /PCM_CLK
- IC2 pad 6: GND -> Net-(IC2-Pad6)
- IC2 pad 7: Net-(IC2-Pad7) -> +3V3
- IC2 pad 8: CM4_SDA4 -> GND
- IC2 pad 9: CM4_SCL4 -> Net-(IC2-Pad9)
- J1 pad 1: Net-(D2-Pad1) -> +3V3
- J1 pad 10: Net-(D1-Pad2) -> /GPIO15
- J1 pad 2: Net-(D2-Pad1) -> +5V
- J1 pad 3: GND -> /SDA1
- J1 pad 4: GND -> +5V
- J1 pad 5: GND -> /SCL1
- J1 pad 7: GND -> /GPIO04
- J1 pad 8: GND -> /GPIO14
- J1 pad 9: Net-(D1-Pad2) -> GND
- J2 pad 2: -12V -> /D9
- J2 pad 3: +12V -> GND
- J2 pad 4: +3V3 -> /D8
- R1 pad 1: +12V -> /CODEC_IN_L
- R1 pad 2: Net-(R1-Pad2) -> /AUDIO_IN_L
- R2 pad 1: Net-(C15-Pad1) -> /CODEC_IN_R
- R2 pad 2: CODEC_VOUT_L- -> /AUDIO_IN_R
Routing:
- net +12V: track 453.6 -> 0.00 mm, vias 5 -> 0
- net +3V3: track 345.2 -> 68.5 mm, vias 4 -> 0
- net -12V: track 267.8 -> 0.00 mm, vias 6 -> 0
- net /CV/VREF_-2.5: track 214.6 -> 0.00 mm
- net GND: track 244.2 -> 38.5 mm, vias 134 -> 13
- net GATE_IN_4: track 153.9 -> 0.00 mm, vias 6 -> 0
- net +5VA: track 152.1 -> 0.00 mm, vias 7 -> 0
- net GATE_IN_3: track 148.6 -> 0.00 mm, vias 4 -> 0
- net GATE_IN_2: track 126.8 -> 0.00 mm, vias 4 -> 0
- net /CV/CH5: track 123.5 -> 0.00 mm, vias 1 -> 0
- net /CV/CH4: track 118.1 -> 0.00 mm, vias 1 -> 0
- net GATE_IN_1: track 109.3 -> 0.00 mm, vias 4 -> 0
- net /CV/CH7: track 106.8 -> 0.00 mm, vias 1 -> 0
- net CODEC_VOUT_R-: track 106.8 -> 0.00 mm, vias 5 -> 0
- net CODEC_VOUT_R+: track 102.0 -> 0.00 mm, vias 4 -> 0
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- added copper zone on B.Cu, net GND
- added copper zone on F.Cu, net GND
- removed copper zone on Gnd.Cu, net GND
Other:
- board size 189 x 145 mm -> 65 x 56 mm
- copper layers 4 -> 2
- net class Default: via_drill 0.25 -> 0.3
